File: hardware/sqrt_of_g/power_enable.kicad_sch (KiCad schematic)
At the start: 7 parts, among them Q3 NDS8434

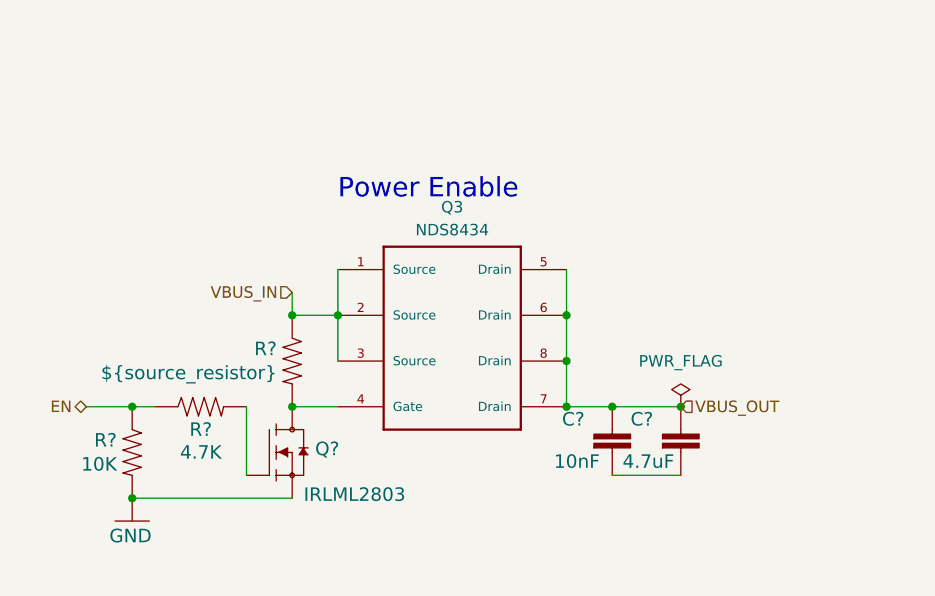
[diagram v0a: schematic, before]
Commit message: fix landing pattern
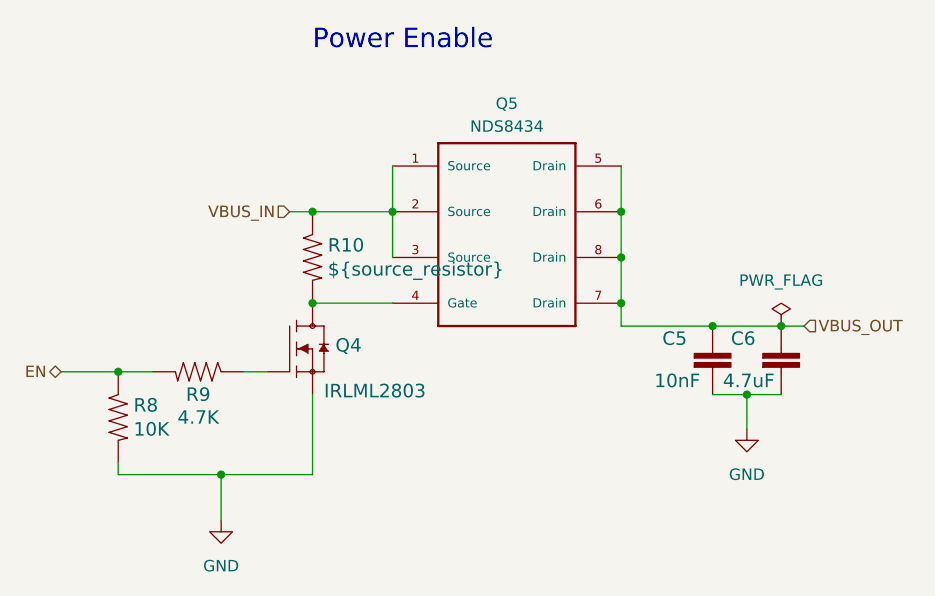
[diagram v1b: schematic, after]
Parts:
- removed Q3: NDS8434, mainboard:NDS8434, symbol adcs:NDS8434
- removed Q?: IRLML2803, mainboard:SOT-23, symbol mainboard:IRLML2803TRPBF
- added Q4: IRLML2803, mainboard:SOT-23, symbol mainboard:IRLML2803TRPBF
- added Q5: NDS8434, mainboard:NDS8434, symbol adcs:NDS8434
- C5, C6: renamed from C?; footprint Capacitor_SMD:C_0603_1608Metric -> Capacitor_SMD:C_0402_1005Metric
- R10, R8, R9: renamed from R?; footprint Resistor_SMD:R_0603_1608Metric -> Resistor_SMD:R_0402_1005Metric
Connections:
- net EN: now also R9.2; no longer R9.1
- net GND: now also C5.2, C6.2, Q4.2 (S)
- net VBUS_IN: now also Q5.1 (Source), Q5.2 (Source), Q5.3 (Source)
- net VBUS_OUT: now also Q5.5 (Drain), Q5.6 (Drain), Q5.7 (Drain), Q5.8 (Drain)
- net at R10.2: now also Q4.3 (D), Q5.4 (Gate)
- new net: Q4.1 (G), R9.1
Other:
- title: (none) -> √g
- moved on the sheet: C5, C6, R10, R8, R9
